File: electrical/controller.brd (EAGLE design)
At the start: 101.6 x 25.4 mm, 33 parts, among them Q1 IRLIB9343PBF-ND, U1 POLOLU_D24V22F5, U2 TPS3710, U3 MCP4725, U4 MCP4725, U5 MCP6002

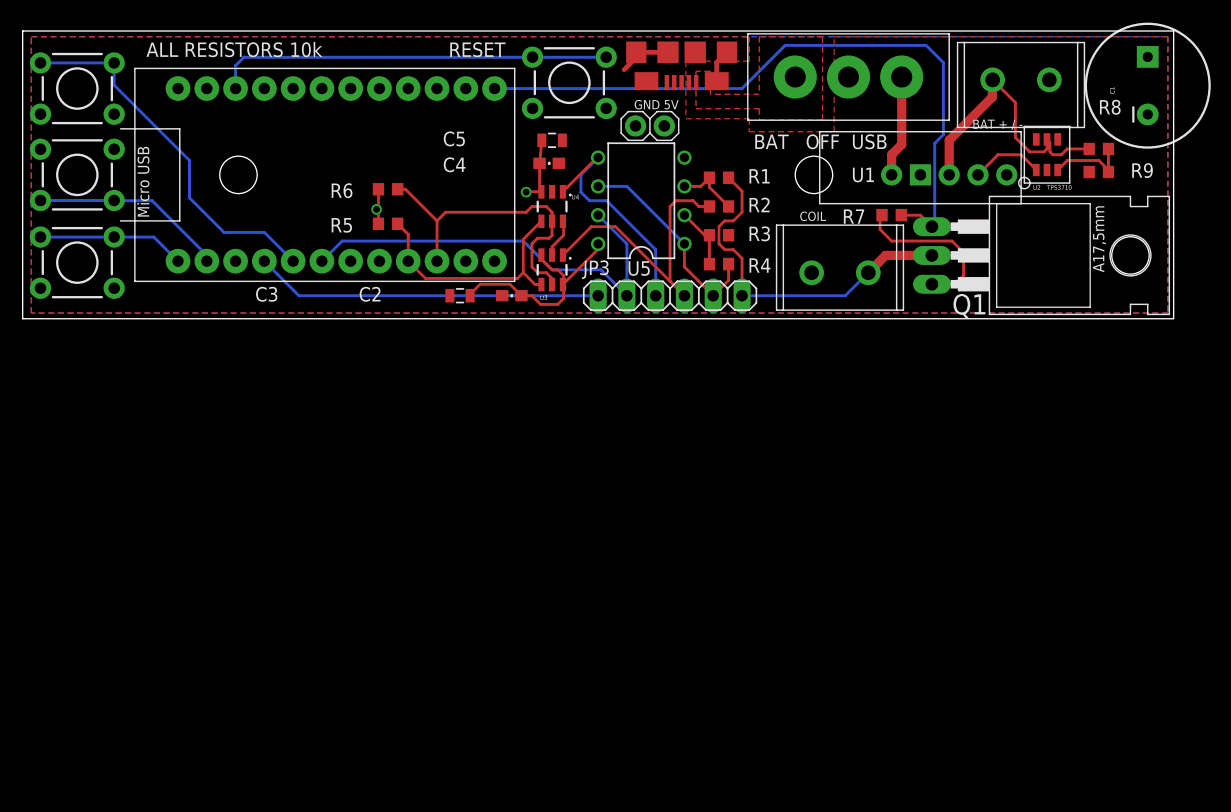
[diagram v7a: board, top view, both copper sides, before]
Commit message: Finally reasonable progress on the electronics
This plus github.

Nearly done fleshing the SCH out.

Routing should not be difficult, just a few hours.

Postponing changing the power parts of this circuit untill after the
spools are done.  Everything but the power, I can do now --> ship a
revision, test it.
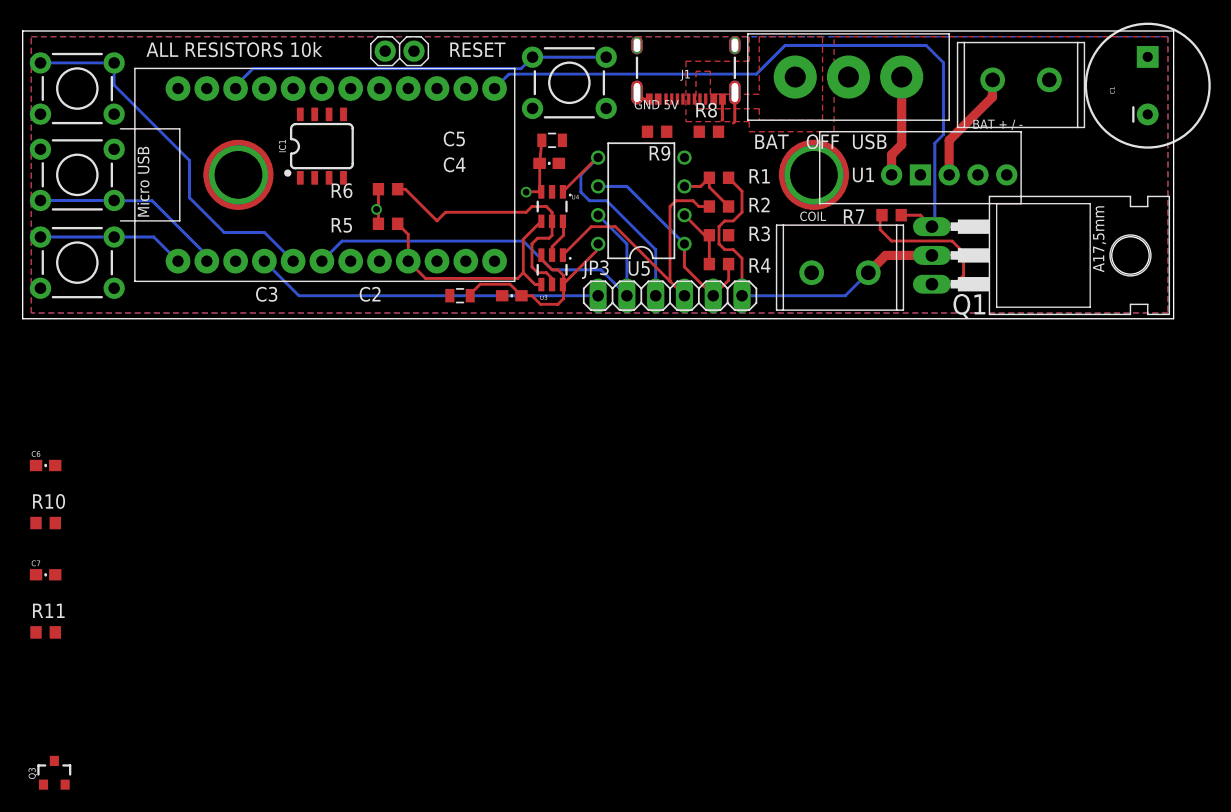
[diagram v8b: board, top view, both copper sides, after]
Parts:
- removed U$12, U$8: (no value), pie:STAND-OFF-TIGHT
- removed U2: TPS3710, custom_parts:SOT6
- removed USB1: USB-OTGMICRO-AB, pie:USB-MICRO-AB
- added C6: 0.01 uF, BEST_Custom:0603-CAP
- added C7: 2.2uf, BEST_Custom:0603-CAP
- added IC1: 555, SparkFun-IC-Special-Function:SO08
- added J1: (no value), SparkFun-Connectors:USB-C-16P-2LAYER-PADS
- added Q3: 600mA/40V, SparkFun-DiscreteSemi:SOT23-3
- added R10: 10K, pie:R0603
- added R11: 2.2M, pie:R0603
- added STANDOFF1, STANDOFF2: STAND-OFFKEYSTONE_SMT_STANDOFF, BEST_Custom:KEYSTONE-4881
- R8: value 115k -> 5.1K
- R9: value 10K -> 5.1K
- U5: value MCP6002 -> MCP6142
- moved R9 39.2 mm to (56.0, 16.5), turned to 180 degrees
- moved R8 34.5 mm to (60.6, 16.5), turned to 0 degrees
- moved JP2 23.1 mm to (33.3, 23.6), turned to 0 degrees
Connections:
- new net AUTO_RESTART: IC1.3, R10.2, UC1.7
- new net CC1: J1.A5, R8.1, UC1.A0
- new net CC2: J1.B5, R9.1, UC1.A1
- new net N$7: C7.2, IC1.6, IC1.7, Q3.2, R11.1
- net 5V: now also IC1.4, IC1.8, R10.1, R11.2
- net DRIVE: now also IC1.2, Q3.1
- net GND: now also C6.2, C7.1, IC1.1, J1.GND, J1.GND2, J1.SHLD1, J1.SHLD2, J1.SHLD3, J1.SHLD4, Q3.3, R8.2, R9.2; no longer R9.1, U2.P2, U2.P4, U2.P6, USB1.P$10, USB1.P$11, USB1.P$5, USB1.P$6, USB1.P$7, USB1.P$8, USB1.P$9
- net N$1: no longer U2.P1
- net N$2: now also J1.VBUS1, J1.VBUS2; no longer USB1.P$1
- net N$6: now also C6.1, IC1.5; no longer R8.1, R9.2, U2.P3
- net SCL: now also UC1.8; no longer UC1.7
- net VBAT: no longer R8.2, U2.P5
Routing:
- net VBAT: track 25.1 -> 9.97 mm
- net N$6: track 7.20 -> 0.00 mm
- net N$1: track 6.45 -> 0.00 mm
- net SCL: track 28.0 -> 24.4 mm
- net GND: track 41.8 -> 40.1 mm
- net RST: track 35.1 -> 34.0 mm
